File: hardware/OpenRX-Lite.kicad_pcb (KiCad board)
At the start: 6 copper layers, 10 x 11.5 mm, 50 parts, among them U1 ESP32-C3, U2 TLV75533PDQNR, U3 SX1281IMLTRT, X1 CJ17-400001010B20

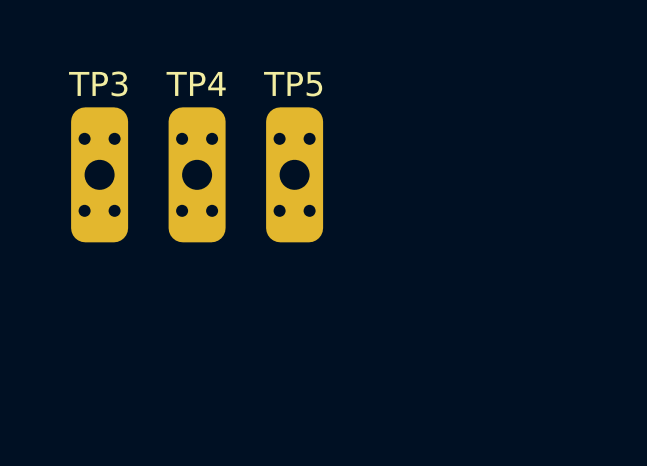
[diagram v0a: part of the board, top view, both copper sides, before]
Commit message: Delete three orphan test pads off the board
TP3, TP4 and TP5 each existed twice. The duplicates sat around 100 mm
from the board, outside Edge.Cuts, and put copper on all six layers plus
15 plated holes into the fabrication data: the shipped Gerbers spanned
X 0.62 to 109.80 against an outline of X 100.00 to 110.00.

The copies on the board keep the +5V, GND, TX, RX and BOOT nets, so the
pads themselves are unchanged and the board now matches OpenRX-Lite-UFL,
which never had the duplicates.

Co-Authored-By: Claude Opus 5 (1M context) <noreply@anthropic.com>
Claude-Session: https://claude.ai/code/session_01HXA6SP2VEuBZn7yMrez3es
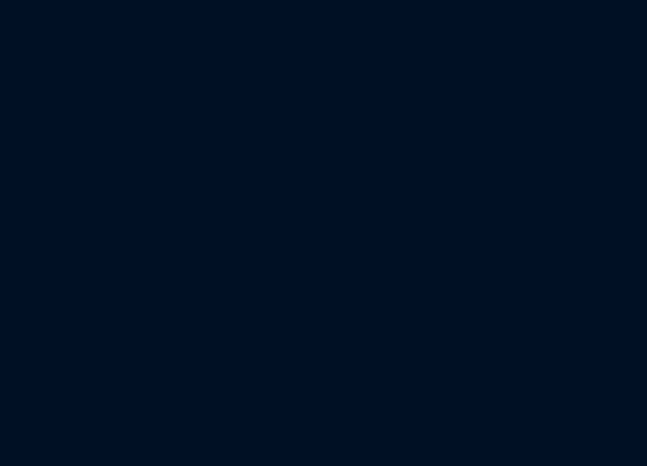
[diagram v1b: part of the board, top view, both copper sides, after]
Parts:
- removed the TP3 at (1.12, 2.42)
- removed the TP4 at (4.38, 2.42)
- removed the TP5 at (7.62, 2.42)
